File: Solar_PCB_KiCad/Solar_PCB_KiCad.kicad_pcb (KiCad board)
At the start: 2 copper layers, 70 x 39 mm, 25 parts, among them J1 Screw_Terminal_01x02, J2 Screw_Terminal_01x02, J3 Screw_Terminal_01x02, U1 LT3652EMSE

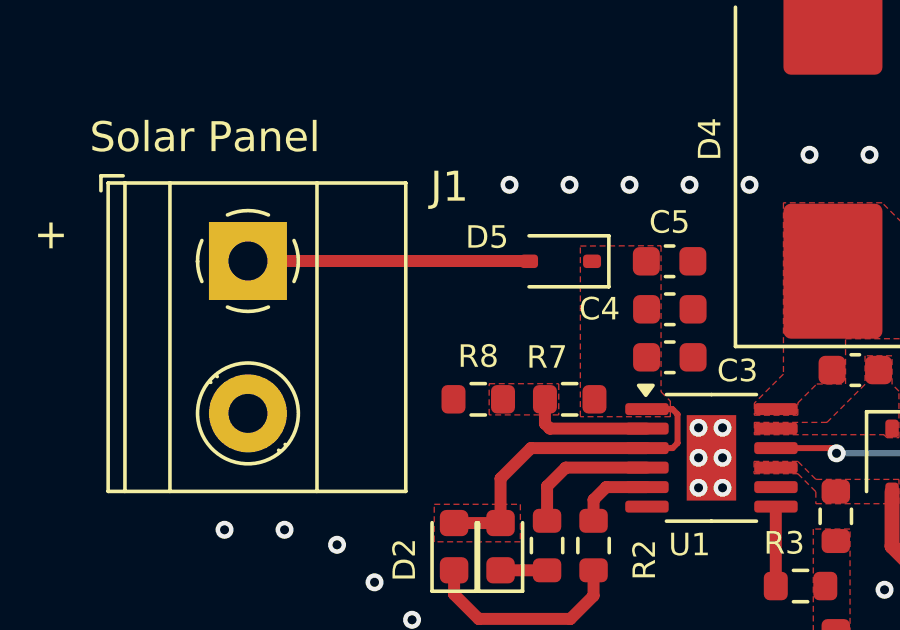
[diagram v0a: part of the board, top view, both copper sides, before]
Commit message: Updated diode + render + thermal considerations
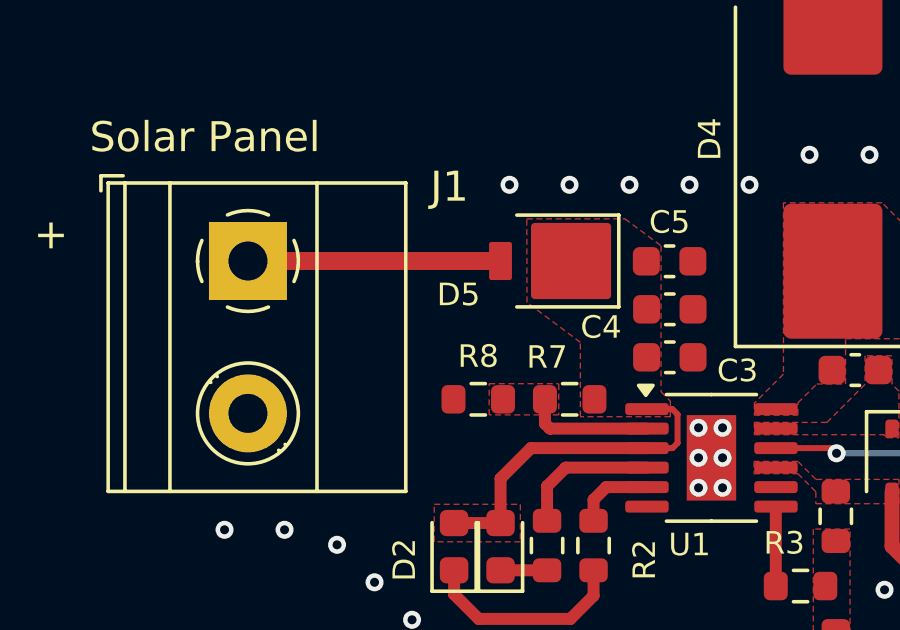
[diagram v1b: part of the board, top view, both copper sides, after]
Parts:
- D5: footprint Diode_SMD:D_SOD-323 -> Diode_SMD:D_SMP_DO-220AA
- moved D5 0.35 mm to (142.4, 109.5)
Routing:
- net Net-(D5-A): track 9.37 -> 8.42 mm
